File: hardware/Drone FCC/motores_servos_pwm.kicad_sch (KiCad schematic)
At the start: 14 parts

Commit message: started schematic
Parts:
- J10, J11, J12, J13, J14, J15, J16, J3, J4, J5, J6, J7, J8, J9: renamed from J?; footprint (none) -> TSW-101-08-G-T-RA:SAMTEC_TSW-101-08-G-T-RA
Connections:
- net PWM1 renamed ESC_1
- net PWM2 renamed ESC_2
- net PWM3 renamed ESC_3
- net PWM4 renamed ESC_4
- net PWM5 renamed ESC_5
- net PWM6 renamed ESC_6

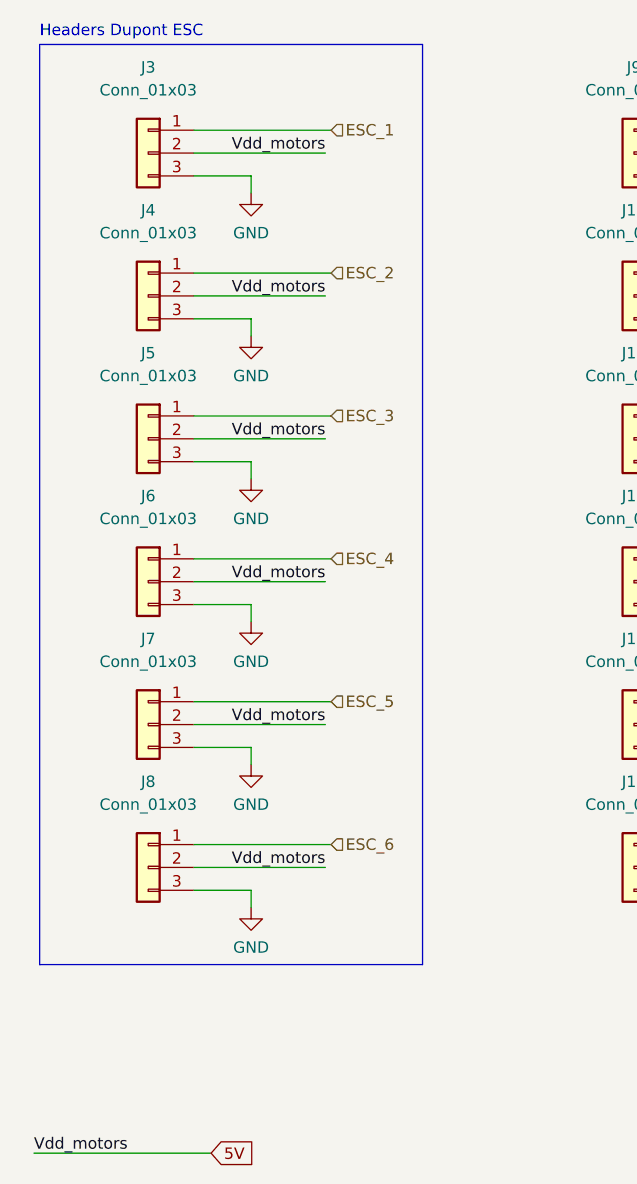
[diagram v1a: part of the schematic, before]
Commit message: add USB connector
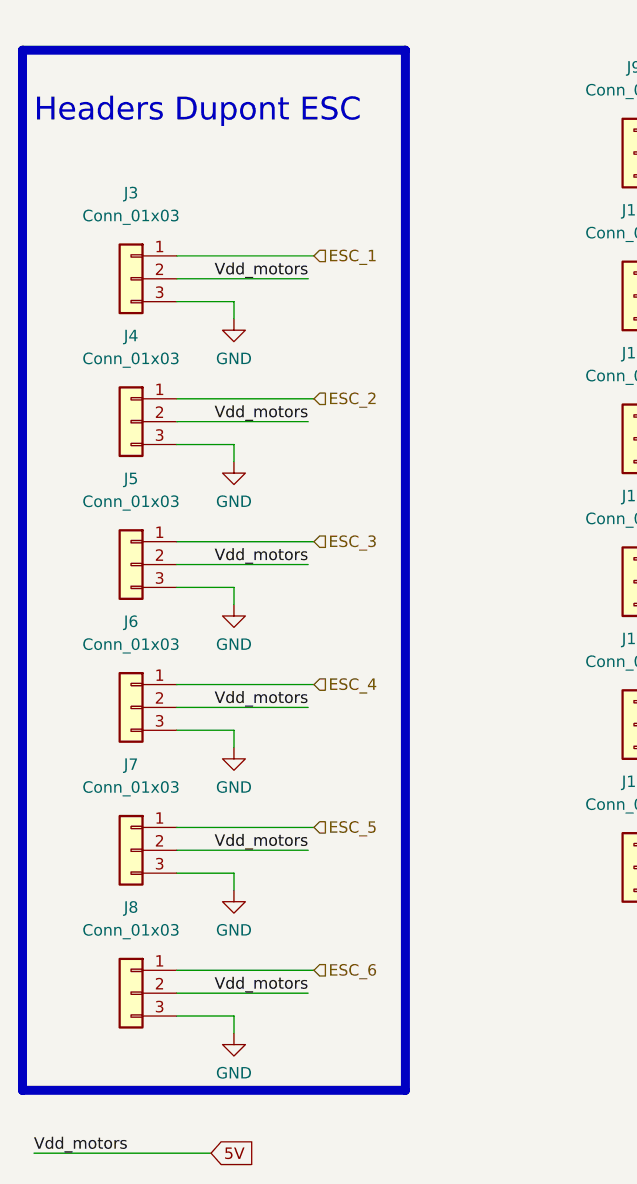
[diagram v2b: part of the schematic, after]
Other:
- moved on the sheet: J3, J4, J5, J6, J7, J8

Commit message: DSM: deleted dupont conn, PPM: deleted DF-13 conn
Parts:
- J10, J11, J12, J13, J14, J15, J16, J9: footprint TSW-101-08-G-T-RA:SAMTEC_TSW-101-08-G-T-RA -> (none)
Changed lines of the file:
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@@
     (property "Reference" "J15" (id 0) (at 174.625 23.495 0))
     (property "Value" "Conn_01x03" (id 1) (at 174.625 26.035 0))
-    (property "Footprint" "TSW-101-08-G-T-RA:SAMTEC_TSW-101-08-G-T-RA" (id 2) (at 174.625 33.02 0)
+    (property "Footprint" "" (id 2) (at 174.625 33.02 0)
       (effects (font (size 1.27 1.27)) hide)
     )
@@
     (property "Reference" "J13" (id 0) (at 124.46 86.995 0))
     (property "Value" "Conn_01x03" (id 1) (at 124.46 89.535 0))
-    (property "Footprint" "TSW-101-08-G-T-RA:SAMTEC_TSW-101-08-G-T-RA" (id 2) (at 124.46 96.52 0)
+    (property "Footprint" "" (id 2) (at 124.46 96.52 0)
       (effects (font (size 1.27 1.27)) hide)
     )
@@
     (property "Reference" "J14" (id 0) (at 124.46 102.87 0))
     (property "Value" "Conn_01x03" (id 1) (at 124.46 105.41 0))
-    (property "Footprint" "TSW-101-08-G-T-RA:SAMTEC_TSW-101-08-G-T-RA" (id 2) (at 124.46 112.395 0)
+    (property "Footprint" "" (id 2) (at 124.46 112.395 0)
       (effects (font (size 1.27 1.27)) hide)
     )
@@
     (property "Reference" "J11" (id 0) (at 124.46 55.245 0))
     (property "Value" "Conn_01x03" (id 1) (at 124.46 57.785 0))
-    (property "Footprint" "TSW-101-08-G-T-RA:SAMTEC_TSW-101-08-G-T-RA" (id 2) (at 124.46 64.77 0)
+    (property "Footprint" "" (id 2) (at 124.46 64.77 0)
       (effects (font (size 1.27 1.27)) hide)
     )
@@
     (property "Reference" "J10" (id 0) (at 124.46 39.37 0))
     (property "Value" "Conn_01x03" (id 1) (at 124.46 41.91 0))
-    (property "Footprint" "TSW-101-08-G-T-RA:SAMTEC_TSW-101-08-G-T-RA" (id 2) (at 124.46 48.895 0)
+    (property "Footprint" "" (id 2) (at 124.46 48.895 0)
       (effects (font (size 1.27 1.27)) hide)
     )
@@
     (property "Reference" "J9" (id 0) (at 124.46 23.495 0))
     (property "Value" "Conn_01x03" (id 1) (at 124.46 26.035 0))
-    (property "Footprint" "TSW-101-08-G-T-RA:SAMTEC_TSW-101-08-G-T-RA" (id 2) (at 124.46 33.02 0)
+    (property "Footprint" "" (id 2) (at 124.46 33.02 0)
       (effects (font (size 1.27 1.27)) hide)
     )
@@
     (property "Reference" "J16" (id 0) (at 174.625 39.37 0))
     (property "Value" "Conn_01x03" (id 1) (at 174.625 41.91 0))
-    (property "Footprint" "TSW-101-08-G-T-RA:SAMTEC_TSW-101-08-G-T-RA" (id 2) (at 174.625 48.895 0)
+    (property "Footprint" "" (id 2) (at 174.625 48.895 0)
       (effects (font (size 1.27 1.27)) hide)
     )
@@
     (property "Reference" "J12" (id 0) (at 124.46 71.12 0))
     (property "Value" "Conn_01x03" (id 1) (at 124.46 73.66 0))
-    (property "Footprint" "TSW-101-08-G-T-RA:SAMTEC_TSW-101-08-G-T-RA" (id 2) (at 124.46 80.645 0)
-      (effects (font (size 1.27 1.27)) hide)
-    )
+    (property "Footprint" "" (id 2) (at 124.46 80.645 0)
+      (effects (font (size 1.27 1.27)) hide)
+    )

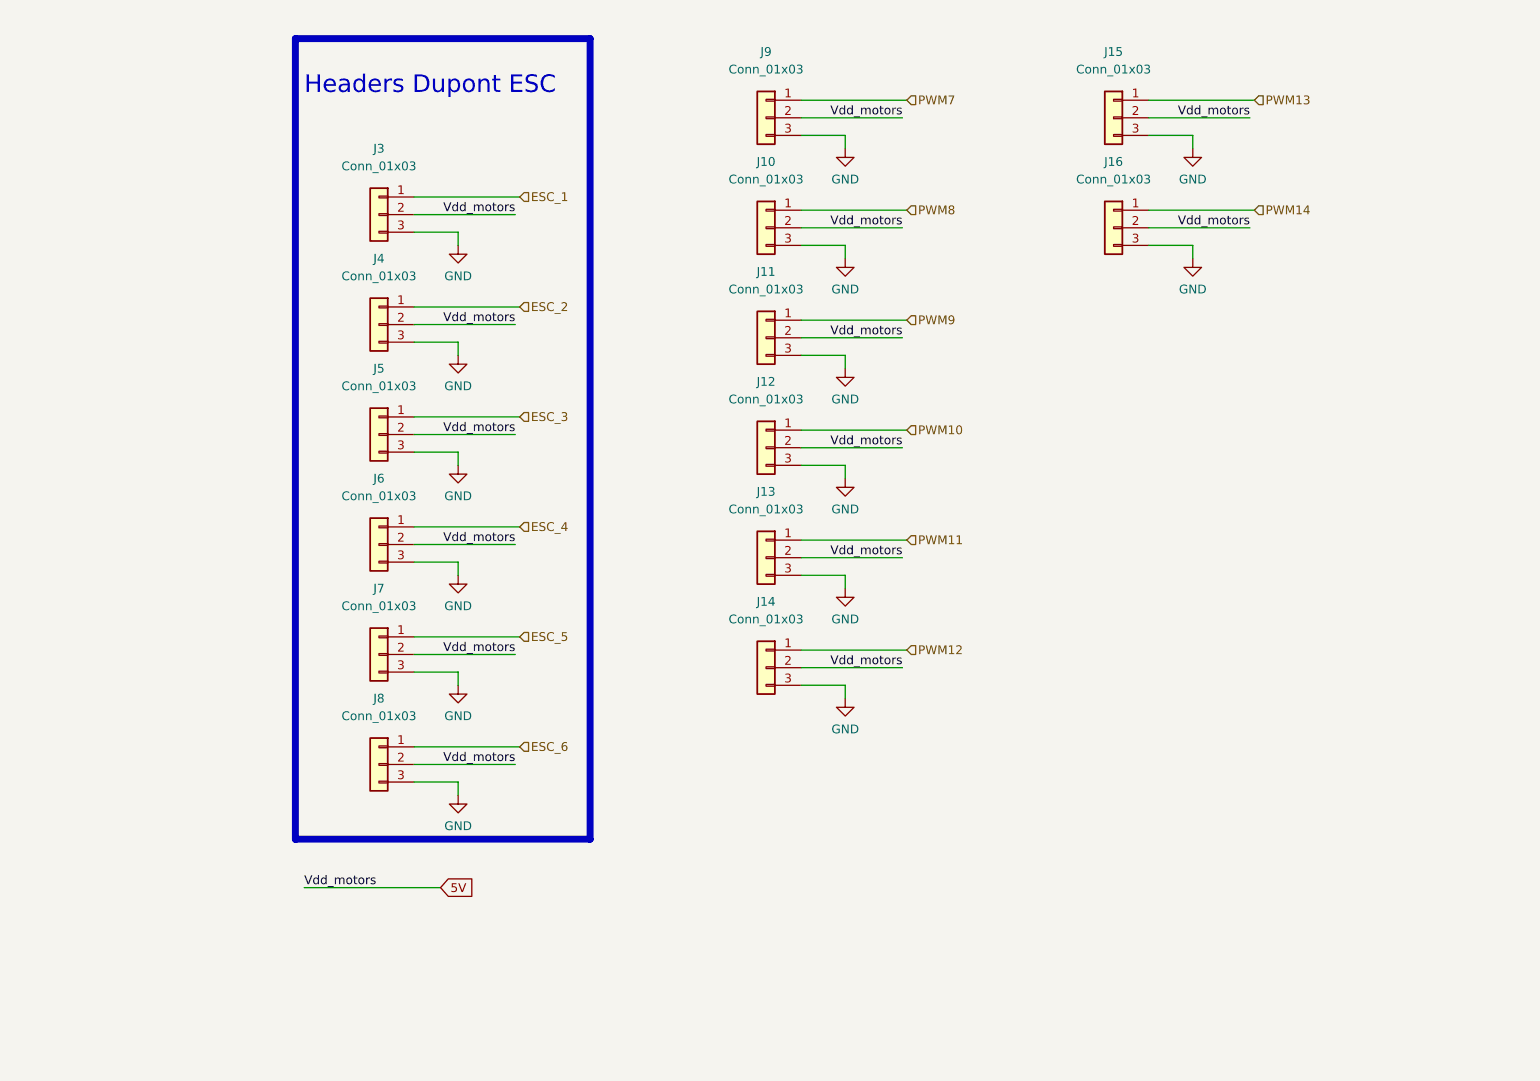
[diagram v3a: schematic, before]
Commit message: rearranged FCC schematic
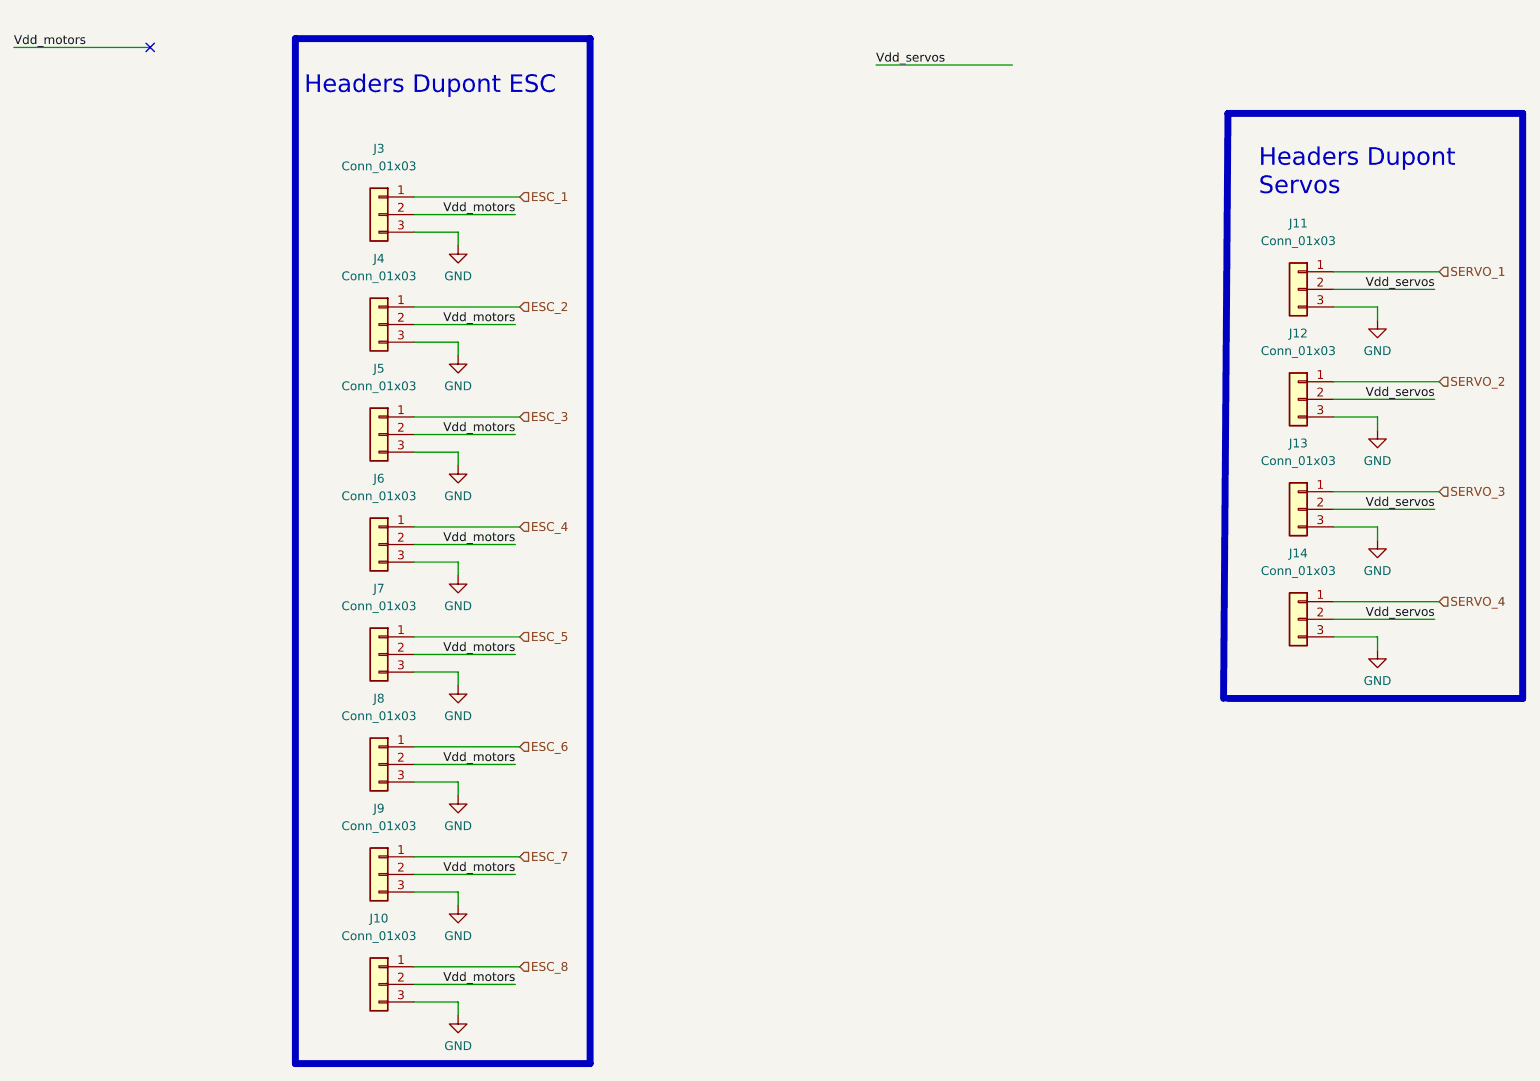
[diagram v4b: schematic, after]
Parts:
- removed J15, J16: Conn_01x03, symbol Connector_Generic:Conn_01x03
- J10, J11, J12, J13, J14, J9: footprint (none) -> TSW-101-08-G-T-RA:SAMTEC_TSW-101-08-G-T-RA
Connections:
- net 5V renamed Vdd_motors
- net Vdd_motors: no longer J11.2 (Pin_2), J12.2 (Pin_2), J13.2 (Pin_2), J14.2 (Pin_2)
- net PWM10 renamed SERVO_2
- net PWM11 renamed SERVO_3
- net PWM12 renamed SERVO_4
- net PWM7 renamed ESC_7
- net PWM8 renamed ESC_8
- net PWM9 renamed SERVO_1
- new net Vdd_servos: J11.2 (Pin_2), J12.2 (Pin_2), J13.2 (Pin_2), J14.2 (Pin_2)
- no-connect marks 0 -> 1
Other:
- note added: "Headers Dupont Servos"
- moved on the sheet: J10, J11, J12, J13, J14, J9

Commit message: add external communication connectors
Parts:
- added J16: Conn_01x02, Connector_Phoenix_MSTB:PhoenixContact_MSTBA_2,5_2-G-5,08_1x02_P5.08mm_Horizontal, symbol Connector_Generic:Conn_01x02
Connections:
- net GND: now also J16.2 (Pin_2)
- net Vdd_servos: now also J16.1 (Pin_1)
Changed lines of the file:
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@@
+    (stroke (width 0) (type default) (color 0 0 0 0))
+  )
+  (wire (pts (xy 160.02 27.94) (xy 157.48 27.94))
     (stroke (width 0) (type default) (color 0 0 0 0))
   )
@@
   )
   (wire (pts (xy 80.01 97.155) (xy 73.66 97.155))
+    (stroke (width 0) (type default) (color 0 0 0 0))
+  )
+  (wire (pts (xy 157.48 27.94) (xy 157.48 31.75))
     (stroke (width 0) (type default) (color 0 0 0 0))
   )
@@
     (pin "3")
   )
+  (symbol (lib_id "Connector_Generic:Conn_01x02") (at 165.1 25.4 0) (unit 1)
+    (in_bom yes) (on_board yes) (fields_autoplaced)
+    (property "Reference" "J16" (id 0) (at 167.64 25.3999 0)
+      (effects (font (size 1.27 1.27)) (justify left))
+    )
+    (property "Value" "Conn_01x02" (id 1) (at 167.64 27.9399 0)
+      (effects (font (size 1.27 1.27)) (justify left))
+    )
+    (property "Footprint" "Connector_Phoenix_MSTB:PhoenixContact_MSTBA_2,5_2-G-5,08_1x02_P5.08mm_Horizontal" (id 2) (at 165.1 25.4 0)
+      (effects (font (size 1.27 1.27)) hide)
+    )
+    (property "Datasheet" "~" (id 3) (at 165.1 25.4 0)
+      (effects (font (size 1.27 1.27)) hide)
+    )
+    (pin "1")
+    (pin "2")
+  )
   (symbol (lib_id "Connector_Generic:Conn_01x03") (at 68.58 142.24 0) (mirror y) (unit 1)
     (in_bom yes) (on_board yes) (fields_autoplaced)
@@
     (pin "3")
   )
+  (symbol (lib_id "power:GND") (at 157.48 31.75 0) (unit 1)
+    (in_bom yes) (on_board yes) (fields_autoplaced)
+    (property "Reference" "#PWR0163" (id 0) (at 157.48 38.1 0)
+      (effects (font (size 1.27 1.27)) hide)
+    )
+    (property "Value" "GND" (id 1) (at 157.48 36.195 0))
+    (property "Footprint" "" (id 2) (at 157.48 31.75 0)
+      (effects (font (size 1.27 1.27)) hide)
+    )
+    (property "Datasheet" "" (id 3) (at 157.48 31.75 0)
+      (effects (font (size 1.27 1.27)) hide)
+    )
+    (pin "1")
+  )
   (symbol (lib_id "power:GND") (at 80.01 51.435 0) (unit 1)
